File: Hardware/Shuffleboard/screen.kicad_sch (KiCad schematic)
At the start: 0 parts

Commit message: fet driving
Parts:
- added J3: Conn_01x10, ShuffleboardFootprints:CES-110-XX-Y-S, symbol Connector_Generic:Conn_01x10
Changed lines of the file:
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@@
 	(generator_version "9.0")
 	(paper "A4")
+	(symbol
+		(lib_id "Connector_Generic:Conn_01x10")
+		(at 38.1 36.83 0)
+		(unit 1)
+		(exclude_from_sim no)
+		(in_bom yes)
+		(on_board yes)
+		(dnp no)
+		(fields_autoplaced yes)
+		(property "Reference" "J3"
+			(at 40.64 36.8299 0)
+			(effects
+				(font
+					(size 1.27 1.27)
+				)
+				(justify left)
+			)
+		)
+		(property "Value" "Conn_01x10"
+			(at 40.64 39.3699 0)
+			(effects
+				(font
+					(size 1.27 1.27)
+				)
+				(justify left)
+			)
+		)
+		(property "Footprint" "ShuffleboardFootprints:CES-110-XX-Y-S"
+			(at 38.1 36.83 0)
+			(effects
+				(font
+					(size 1.27 1.27)
+				)
+				(hide yes)
+			)
+		)
+		(property "Datasheet" "https://www.mouser.com/datasheet/3/85/1/ces.pdf"
+			(at 38.1 36.83 0)
+			(effects
+				(font
+					(size 1.27 1.27)
+				)
+				(hide yes)
+			)
+		)
+		(property "Description" "Generic connector, single row, 01x10, script generated (kicad-library-utils/schlib/autogen/connector/)"
+			(at 38.1 36.83 0)
+			(effects
+				(font
+					(size 1.27 1.27)
+				)
+				(hide yes)
+			)
+		)
+		(property "Mouser Link" "https://www.mouser.com/ProductDetail/Samtec/CES-110-01-G-S?qs=0lQeLiL1qybgWSOLyEsrIw%3D%3D"
+			(at 38.1 36.83 0)
+			(effects
+				(font
+					(size 1.27 1.27)
+				)
+				(hide yes)
+			)
+		)
+		(property "Mouser Part Number" "200-CES11001GS"
+			(at 38.1 36.83 0)
+			(effects
+				(font
+					(size 1.27 1.27)
+				)
+				(hide yes)
+			)
+		)
+		(pin "8"
+		)
+		(pin "7"
+		)
+		(pin "4"
+		)
+		(pin "5"
+		)
+		(pin "6"
+		)
+		(pin "10"
+		)
+		(pin "3"
+		)
+		(pin "2"
+		)
+		(pin "1"
+		)
+		(pin "9"
+		)
+		(instances
+			(project ""
+				(path "/8d05e546-da1a-40d0-9e47-08c4b800bb0e/cb2e7e6c-b6e5-4b1e-adea-6829899b3c9f"
+					(reference "J3")
+					(unit 1)
+				)
+			)
+		)
+	)
 )

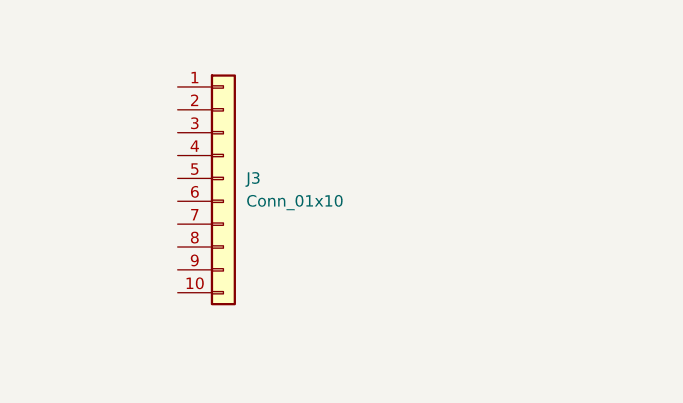
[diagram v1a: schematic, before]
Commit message: footprint for lcd
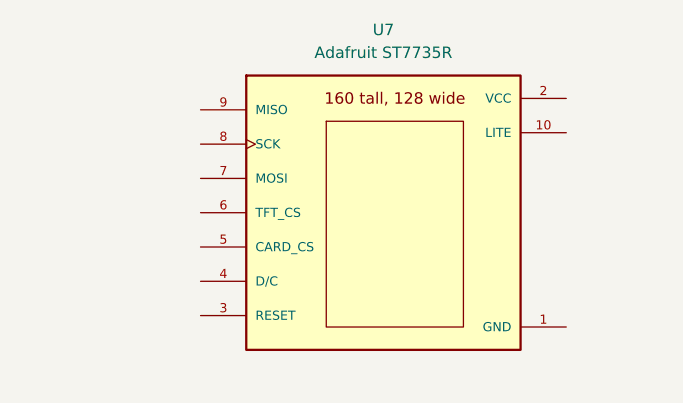
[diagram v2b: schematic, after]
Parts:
- removed J3: Conn_01x10, ShuffleboardFootprints:CES-110-XX-Y-S, symbol Connector_Generic:Conn_01x10
- added U7: Adafruit ST7735R, Footprint:adafruit_st7735r, symbol ECE319:Adafruit_ST7735R
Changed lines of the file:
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@@
 	(paper "A4")
 	(symbol
-		(lib_id "Connector_Generic:Conn_01x10")
-		(at 38.1 36.83 0)
+		(lib_id "ECE319:Adafruit_ST7735R")
+		(at 55.88 40.64 0)
 		(unit 1)
 		(exclude_from_sim no)
@@
 		(dnp no)
 		(fields_autoplaced yes)
-		(property "Reference" "J3"
-			(at 40.64 36.8299 0)
+		(property "Reference" "U7"
+			(at 55.88 20.32 0)
 			(effects
 				(font
 					(size 1.27 1.27)
 				)
-				(justify left)
 			)
 		)
-		(property "Value" "Conn_01x10"
-			(at 40.64 39.3699 0)
+		(property "Value" "Adafruit ST7735R"
+			(at 55.88 22.86 0)
 			(effects
 				(font
 					(size 1.27 1.27)
 				)
-				(justify left)
 			)
 		)
-		(property "Footprint" "ShuffleboardFootprints:CES-110-XX-Y-S"
-			(at 38.1 36.83 0)
+		(property "Footprint" "Footprint:adafruit_st7735r"
+			(at 50.8 17.78 0)
+			(effects
+				(font
+					(size 1.27 1.27)
+				)
+				(justify bottom)
+				(hide yes)
+			)
+		)
+		(property "Datasheet" "https://www.mouser.com/datasheet/2/737/ST7735R_V0_2-2489618.pdf"
+			(at 54.61 21.59 0)
 			(effects
 				(font
@@
 			)
 		)
-		(property "Datasheet" "https://www.mouser.com/datasheet/3/85/1/ces.pdf"
-			(at 38.1 36.83 0)
+		(property "Description" ""
+			(at 55.88 40.64 0)
 			(effects
 				(font
@@
 			)
 		)
-		(property "Description" "Generic connector, single row, 01x10, script generated (kicad-library-utils/schlib/autogen/connector/)"
-			(at 38.1 36.83 0)
+		(property "Distributor" "Mouser"
+			(at 55.88 19.05 0)
 			(effects
 				(font
@@
 			)
 		)
-		(property "Mouser Link" "https://www.mouser.com/ProductDetail/Samtec/CES-110-01-G-S?qs=0lQeLiL1qybgWSOLyEsrIw%3D%3D"
-			(at 38.1 36.83 0)
+		(property "Manufacturer" "Adafruit"
+			(at 40.64 19.05 0)
 			(effects
 				(font
@@
 			)
 		)
-		(property "Mouser Part Number" "200-CES11001GS"
-			(at 38.1 36.83 0)
+		(property "P/N" "358"
+			(at 54.61 24.13 0)
 			(effects
 				(font
@@
 			)
 		)
-		(pin "8"
+		(property "LCSC Part #" ""
+			(at 55.88 40.64 0)
+			(effects
+				(font
+					(size 1.27 1.27)
+				)
+				(hide yes)
+			)
+		)
+		(property "Cost" "19.95"
+			(at 67.31 17.78 0)
+			(effects
+				(font
+					(size 1.27 1.27)
+				)
+				(hide yes)
+			)
+		)
+		(pin "1"
 		)
 		(pin "7"
 		)
-		(pin "4"
+		(pin "3"
+		)
+		(pin "9"
+		)
+		(pin "6"
+		)
+		(pin "8"
 		)
 		(pin "5"
 		)
-		(pin "6"
+		(pin "2"
 		)
 		(pin "10"
 		)
-		(pin "3"
-		)
-		(pin "2"
-		)
-		(pin "1"
-		)
-		(pin "9"
+		(pin "4"
 		)
 		(instances
-			(project ""
+			(project "Shuffleboard"
 				(path "/8d05e546-da1a-40d0-9e47-08c4b800bb0e/cb2e7e6c-b6e5-4b1e-adea-6829899b3c9f"
-					(reference "J3")
+					(reference "U7")
 					(unit 1)
 				)

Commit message: Finished Screen
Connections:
- net GND: now reaches U7.1 (GND)
- net +3.3V: now reaches U7.10 (LITE)
- net +3.3V: now also U7.2 (VCC)
- net PB15_RESET: now reaches U7.3 (RESET)
- net PA13_DC: now reaches U7.4 (D/C)
- net PB6_TFT_CS: now reaches U7.6 (TFT_CS)
- net PB8_MOSI(PICO): now reaches U7.7 (MOSI)
- net PB9_SPI_CLK: now reaches U7.8 (SCK)
- net PB7_MISO(POCI): now reaches U7.9 (MISO)
- no-connect marks 0 -> 1

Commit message: finished layout
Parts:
- U7: value Adafruit ST7735R -> (none)
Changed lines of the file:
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@@
 (kicad_sch
-	(version 20250114)
+	(version 20260306)
 	(generator "eeschema")
-	(generator_version "9.0")
+	(generator_version "10.0")
 	(paper "A4")
 	(no_connect
@@
 		(at 76.2 53.34 0)
 		(unit 1)
+		(body_style 1)
 		(exclude_from_sim no)
 		(in_bom yes)
 		(on_board yes)
+		(in_pos_files yes)
 		(dnp no)
 		(fields_autoplaced yes)
 		(property "Reference" "#PWR052"
 			(at 76.2 59.69 0)
-			(effects
-				(font
-					(size 1.27 1.27)
-				)
-				(hide yes)
+			(hide yes)
+			(show_name no)
+			(do_not_autoplace no)
+			(effects
+				(font
+					(size 1.27 1.27)
+				)
 			)
 		)
 		(property "Value" "GND"
 			(at 76.2 58.42 0)
+			(show_name no)
+			(do_not_autoplace no)
 			(effects
 				(font
@@
 		(property "Footprint" ""
 			(at 76.2 53.34 0)
-			(effects
-				(font
-					(size 1.27 1.27)
-				)
-				(hide yes)
+			(hide yes)
+			(show_name no)
+			(do_not_autoplace no)
+			(effects
+				(font
+					(size 1.27 1.27)
+				)
 			)
 		)
 		(property "Datasheet" ""
 			(at 76.2 53.34 0)
-			(effects
-				(font
-					(size 1.27 1.27)
-				)
-				(hide yes)
+			(hide yes)
+			(show_name no)
+			(do_not_autoplace no)
+			(effects
+				(font
+					(size 1.27 1.27)
+				)
 			)
 		)
 		(property "Description" "Power symbol creates a global label with name \"GND\" , ground"
 			(at 76.2 53.34 0)
-			(effects
-				(font
-					(size 1.27 1.27)
-				)
-				(hide yes)
+			(hide yes)
+			(show_name no)
+			(do_not_autoplace no)
+			(effects
+				(font
+					(size 1.27 1.27)
+				)
 			)
 		)
@@
 		)
 		(instances
-			(project ""
+			(project "Shuffleboard"
 				(path "/8d05e546-da1a-40d0-9e47-08c4b800bb0e/cb2e7e6c-b6e5-4b1e-adea-6829899b3c9f"
 					(reference "#PWR052")
@@
 		(at 76.2 27.94 270)
 		(unit 1)
+		(body_style 1)
 		(exclude_from_sim no)
 		(in_bom yes)
 		(on_board yes)
+		(in_pos_files yes)
 		(dnp no)
 		(fields_autoplaced yes)
 		(property "Reference" "#PWR054"
 			(at 72.39 27.94 0)
-			(effects
-				(font
-					(size 1.27 1.27)
-				)
-				(hide yes)
+			(hide yes)
+			(show_name no)
+			(do_not_autoplace no)
+			(effects
+				(font
+					(size 1.27 1.27)
+				)
 			)
 		)
 		(property "Value" "+3.3V"
 			(at 80.01 27.9399 90)
+			(show_name no)
+			(do_not_autoplace no)
 			(effects
 				(font
@@
 		(property "Footprint" ""
 			(at 76.2 27.94 0)
-			(effects
-				(font
-					(size 1.27 1.27)
-				)
-				(hide yes)
+			(hide yes)
+			(show_name no)
+			(do_not_autoplace no)
+			(effects
+				(font
+					(size 1.27 1.27)
+				)
 			)
 		)
 		(property "Datasheet" ""
 			(at 76.2 27.94 0)
-			(effects
-				(font
-					(size 1.27 1.27)
-				)
-				(hide yes)
+			(hide yes)
+			(show_name no)
+			(do_not_autoplace no)
+			(effects
+				(font
+					(size 1.27 1.27)
+				)
 			)
 		)
 		(property "Description" "Power symbol creates a global label with name \"+3.3V\""
 			(at 76.2 27.94 0)
-			(effects
-				(font
-					(size 1.27 1.27)
-				)
-				(hide yes)
+			(hide yes)
+			(show_name no)
+			(do_not_autoplace no)
+			(effects
+				(font
+					(size 1.27 1.27)
+				)
 			)
 		)
@@
 		(at 76.2 31.75 270)
 		(unit 1)
+		(body_style 1)
 		(exclude_from_sim no)
 		(in_bom yes)
 		(on_board yes)
+		(in_pos_files yes)
 		(dnp no)
 		(fields_autoplaced yes)
 		(property "Reference" "#PWR053"
 			(at 72.39 31.75 0)
-			(effects
-				(font
-					(size 1.27 1.27)
-				)
-				(hide yes)
+			(hide yes)
+			(show_name no)
+			(do_not_autoplace no)
+			(effects
+				(font
+					(size 1.27 1.27)
+				)
 			)
 		)
 		(property "Value" "+3.3V"
 			(at 80.01 31.7499 90)
+			(show_name no)
+			(do_not_autoplace no)
 			(effects
 				(font
@@
 		(property "Footprint" ""
 			(at 76.2 31.75 0)
-			(effects
-				(font
-					(size 1.27 1.27)
-				)
-				(hide yes)
+			(hide yes)
+			(show_name no)
+			(do_not_autoplace no)
+			(effects
+				(font
+					(size 1.27 1.27)
+				)
 			)
 		)
 		(property "Datasheet" ""
 			(at 76.2 31.75 0)
-			(effects
-				(font
-					(size 1.27 1.27)
-				)
-				(hide yes)
+			(hide yes)
+			(show_name no)
+			(do_not_autoplace no)
+			(effects
+				(font
+					(size 1.27 1.27)
+				)
 			)
 		)
 		(property "Description" "Power symbol creates a global label with name \"+3.3V\""
 			(at 76.2 31.75 0)
-			(effects
-				(font
-					(size 1.27 1.27)
-				)
-				(hide yes)
+			(hide yes)
+			(show_name no)
+			(do_not_autoplace no)
+			(effects
+				(font
+					(size 1.27 1.27)
+				)
 			)
 		)
@@
 		)
 		(instances
-			(project ""
+			(project "Shuffleboard"
 				(path "/8d05e546-da1a-40d0-9e47-08c4b800bb0e/cb2e7e6c-b6e5-4b1e-adea-6829899b3c9f"
 					(reference "#PWR053")
@@
 		(at 55.88 40.64 0)
 		(unit 1)
+		(body_style 1)
 		(exclude_from_sim no)
 		(in_bom yes)
 		(on_board yes)
+		(in_pos_files yes)
 		(dnp no)
 		(fields_autoplaced yes)
 		(property "Reference" "U7"
 			(at 55.88 20.32 0)
-			(effects
-				(font
-					(size 1.27 1.27)
-				)
-			)
-		)
-		(property "Value" "Adafruit ST7735R"
-			(at 55.88 22.86 0)
+			(show_name no)
+			(do_not_autoplace no)
+			(effects
+				(font
+					(size 1.27 1.27)
+				)
+			)
+		)
+		(property "Value" ""
+			(at 55.88 40.64 0)
+			(hide yes)
+			(show_name no)
+			(do_not_autoplace no)
 			(effects
 				(font
@@
 		(property "Footprint" "Footprint:adafruit_st7735r"
 			(at 50.8 17.78 0)
+			(hide yes)
+			(show_name no)
+			(do_not_autoplace no)
 			(effects
 				(font
@@
 				)
 				(justify bottom)
-				(hide yes)
 			)
 		)
 		(property "Datasheet" "https://www.mouser.com/datasheet/2/737/ST7735R_V0_2-2489618.pdf"
 			(at 54.61 21.59 0)
-			(effects
-				(font
-					(size 1.27 1.27)
-				)
-				(hide yes)
+			(hide yes)
+			(show_name no)
+			(do_not_autoplace no)
+			(effects
+				(font
+					(size 1.27 1.27)
+				)
 			)
 		)
 		(property "Description" ""
 			(at 55.88 40.64 0)
-			(effects
-				(font
-					(size 1.27 1.27)
-				)
-				(hide yes)
+			(hide yes)
+			(show_name no)
+			(do_not_autoplace no)
+			(effects
+				(font
+					(size 1.27 1.27)
+				)
 			)
 		)
 		(property "Distributor" "Mouser"
 			(at 55.88 19.05 0)
-			(effects
-				(font
-					(size 1.27 1.27)
-				)
-				(hide yes)
+			(hide yes)
+			(show_name no)
+			(do_not_autoplace no)
+			(effects
+				(font
+					(size 1.27 1.27)
+				)
 			)
 		)
 		(property "Manufacturer" "Adafruit"
 			(at 40.64 19.05 0)
-			(effects
-				(font
-					(size 1.27 1.27)
-				)
-				(hide yes)
+			(hide yes)
+			(show_name no)
+			(do_not_autoplace no)
+			(effects
+				(font
+					(size 1.27 1.27)
+				)
 			)
 		)
 		(property "P/N" "358"
 			(at 54.61 24.13 0)
-			(effects
-				(font
-					(size 1.27 1.27)
-				)
-				(hide yes)
+			(hide yes)
+			(show_name no)
+			(do_not_autoplace no)
+			(effects
+				(font
+					(size 1.27 1.27)
+				)
 			)
 		)
 		(property "LCSC Part #" ""
 			(at 55.88 40.64 0)
-			(effects
-				(font
-					(size 1.27 1.27)
-				)
-				(hide yes)
+			(hide yes)
+			(show_name no)
+			(do_not_autoplace no)
+			(effects
+				(font
+					(size 1.27 1.27)
+				)
 			)
 		)
 		(property "Cost" "19.95"
 			(at 67.31 17.78 0)
-			(effects
-				(font
-					(size 1.27 1.27)
-				)
-				(hide yes)
-			)
-		)
+			(hide yes)
+			(show_name no)
+			(do_not_autoplace no)
+			(effects
+				(font
+					(size 1.27 1.27)
+				)
+			)
+		)

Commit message: tht resistors
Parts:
- U7: now left out of the parts list
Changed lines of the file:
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@@
 		(body_style 1)
 		(exclude_from_sim no)
-		(in_bom yes)
+		(in_bom no)
 		(on_board yes)
 		(in_pos_files yes)
@@
 			(hide yes)
 			(show_name no)
+			(do_not_autoplace no)
+			(effects
+				(font
+					(size 1.27 1.27)
+				)
+			)
+		)
+		(property "VALUE" ""
+			(at 55.88 40.64 0)
+			(hide yes)
+			(show_name no)
